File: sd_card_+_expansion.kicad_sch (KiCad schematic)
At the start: 13 parts, among them J4 Micro_SD_Card_Det1, J7 Conn_02x05_Odd_Even

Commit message: Updates
Routing updates, placed expansion connector.
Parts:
- J7: footprint Connector_PinHeader_2.54mm:PinHeader_2x05_P2.54mm_Vertical -> Connector_PinHeader_2.54mm:PinHeader_2x05_P2.54mm_Vertical_SMD
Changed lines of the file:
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@@
 			)
 		)
-		(property "Footprint" "Connector_PinHeader_2.54mm:PinHeader_2x05_P2.54mm_Vertical"
+		(property "Footprint" "Connector_PinHeader_2.54mm:PinHeader_2x05_P2.54mm_Vertical_SMD"
 			(at 48.26 38.1 0)
 			(effects

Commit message: Bom updates
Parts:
- D3: MPN (none) -> MBR0530T1G; Package (none) -> SOD-123
- F4: MPN (none) -> 0ZCJ0025FF2E; Package (none) -> 1206
- J4: MPN (none) -> DM3D-SF
- J7: now not fitted
- R19, R20, R21, R23: MPN (none) -> RC0402FR-070RL; Package (none) -> 0402
- R22: MPN (none) -> RC0402JR-074K7L; Package (none) -> 0402
- R37, R38, R39, R40: MPN (none) -> RC0402JR-0710KL; Package (none) -> 0402
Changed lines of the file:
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@@
+			)
+		)
+		(property "MPN" "DM3D-SF"
+			(at 246.38 57.15 0)
+			(effects
+				(font
+					(size 1.27 1.27)
+				)
+				(hide yes)
 			)
 		)
@@
 		)
 		(property "Description" "Resistor, small US symbol"
+			(at 210.82 69.85 0)
+			(effects
+				(font
+					(size 1.27 1.27)
+				)
+				(hide yes)
+			)
+		)
+		(property "Package" "0402"
+			(at 210.82 69.85 0)
+			(effects
+				(font
+					(size 1.27 1.27)
+				)
+				(hide yes)
+			)
+		)
+		(property "MPN" "RC0402JR-074K7L"
 			(at 210.82 69.85 0)
 			(effects
@@
 			)
 		)
+		(property "Package" "0402"
+			(at 214.63 62.23 0)
+			(effects
+				(font
+					(size 1.27 1.27)
+				)
+				(hide yes)
+			)
+		)
+		(property "MPN" "RC0402FR-070RL"
+			(at 214.63 62.23 0)
+			(effects
+				(font
+					(size 1.27 1.27)
+				)
+				(hide yes)
+			)
+		)
 		(pin "1"
 		)
@@
 		)
 		(property "Description" "Schottky diode"
+			(at 38.1 54.61 0)
+			(effects
+				(font
+					(size 1.27 1.27)
+				)
+				(hide yes)
+			)
+		)
+		(property "MPN" "MBR0530T1G"
+			(at 38.1 54.61 0)
+			(effects
+				(font
+					(size 1.27 1.27)
+				)
+				(hide yes)
+			)
+		)
+		(property "Package" "SOD-123"
 			(at 38.1 54.61 0)
 			(effects
@@
 			)
 		)
+		(property "Package" "0402"
+			(at 214.63 49.53 0)
+			(effects
+				(font
+					(size 1.27 1.27)
+				)
+				(hide yes)
+			)
+		)
+		(property "MPN" "RC0402FR-070RL"
+			(at 214.63 49.53 0)
+			(effects
+				(font
+					(size 1.27 1.27)
+				)
+				(hide yes)
+			)
+		)
 		(pin "1"
 		)
@@
 			)
 		)
+		(property "Package" "0402"
+			(at 73.66 26.67 0)
+			(effects
+				(font
+					(size 1.27 1.27)
+				)
+				(hide yes)
+			)
+		)
+		(property "MPN" "RC0402JR-0710KL"
+			(at 73.66 26.67 0)
+			(effects
+				(font
+					(size 1.27 1.27)
+				)
+				(hide yes)
+			)
+		)
 		(pin "2"
 		)
@@
 			)
 		)
+		(property "MPN" "0ZCJ0025FF2E"
+			(at 30.48 48.26 0)
+			(effects
+				(font
+					(size 1.27 1.27)
+				)
+				(hide yes)
+			)
+		)
+		(property "Package" "1206"
+			(at 30.48 48.26 0)
+			(effects
+				(font
+					(size 1.27 1.27)
+				)
+				(hide yes)
+			)
+		)
 		(pin "2"
 		)
@@
 		)
 		(property "Description" "Resistor, small US symbol"
+			(at 214.63 52.07 0)
+			(effects
+				(font
+					(size 1.27 1.27)
+				)
+				(hide yes)
+			)
+		)
+		(property "Package" "0402"
+			(at 214.63 52.07 0)
+			(effects
+				(font
+					(size 1.27 1.27)
+				)
+				(hide yes)
+			)
+		)
+		(property "MPN" "RC0402FR-070RL"
 			(at 214.63 52.07 0)
 			(effects
@@
 			)
 		)
+		(property "Package" "0402"
+			(at 69.85 26.67 0)
+			(effects
+				(font
+					(size 1.27 1.27)
+				)
+				(hide yes)
+			)
+		)
+		(property "MPN" "RC0402JR-0710KL"
+			(at 69.85 26.67 0)
+			(effects
+				(font
+					(size 1.27 1.27)
+				)
+				(hide yes)
+			)
+		)
 		(pin "2"
 		)
@@
 			)
 		)
+		(property "Package" "0402"
+			(at 27.94 26.67 0)
+			(effects
+				(font
+					(size 1.27 1.27)
+				)
+				(hide yes)
+			)
+		)
+		(property "MPN" "RC0402JR-0710KL"
+			(at 27.94 26.67 0)
+			(effects
+				(font
+					(size 1.27 1.27)
+				)
+				(hide yes)
+			)
+		)
 		(pin "2"
 		)
@@
 			)
 		)
+		(property "Package" "0402"
+			(at 214.63 57.15 0)
+			(effects
+				(font
+					(size 1.27 1.27)
+				)
+				(hide yes)
+			)
+		)
+		(property "MPN" "RC0402FR-070RL"
+			(at 214.63 57.15 0)
+			(effects
+				(font
+					(size 1.27 1.27)
+				)
+				(hide yes)
+			)
+		)
 		(pin "1"
 		)
@@
 		(in_bom yes)
 		(on_board yes)
-		(dnp no)
+		(dnp yes)
 		(fields_autoplaced yes)
 		(property "Reference" "J7"
@@
 			(at 204.47 45.72 0)
 			(effects
+				(font
+					(size 1.27 1.27)
+				)
+				(hide yes)
+			)
+		)
+		(property "Package" "0402"
+			(at 204.47 45.72 0)
+			(effects
+				(font
+					(size 1.27 1.27)
+				)
+				(hide yes)
+			)
+		)
+		(property "MPN" "RC0402JR-0710KL"
+			(at 204.47 45.72 0)
+			(effects

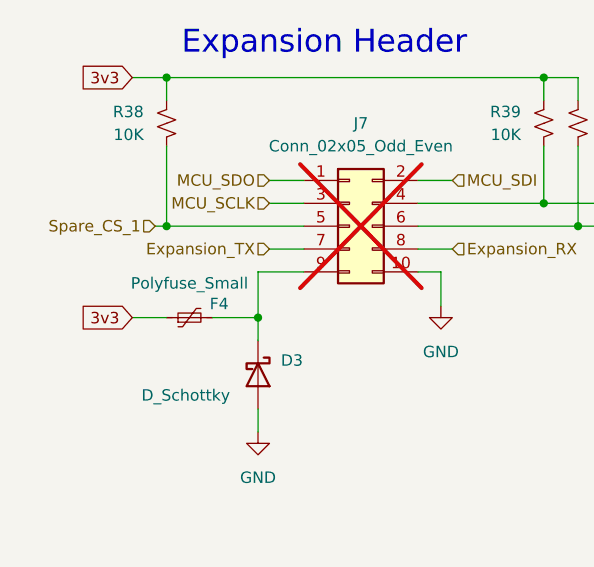
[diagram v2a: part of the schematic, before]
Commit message: Launch day
Completed BOM, added silk art
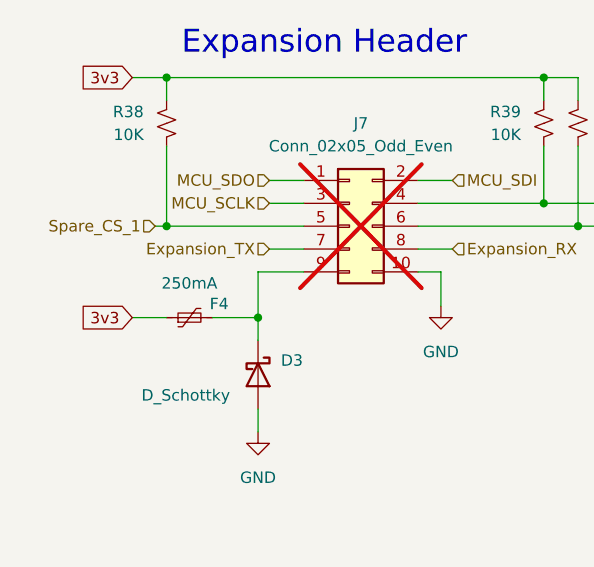
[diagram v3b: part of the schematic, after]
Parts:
- F4: value Polyfuse_Small -> 250mA
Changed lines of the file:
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@@
 			)
 		)
-		(property "Value" "Polyfuse_Small"
+		(property "Value" "250mA"
 			(at 30.48 44.45 90)
 			(effects
